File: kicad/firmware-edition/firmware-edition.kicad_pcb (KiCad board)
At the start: 2 copper layers, 109 parts, among them J1 Solar Panel, J10 GPIO, J11 I2C-3V3, J12 GPIO, J13 SPI, J14 I2C-5V, J15 SWD, J16 Conn_01x01_Pin, J17 Conn_01x01_Pin, J18 Conn_01x01_Pin, J19 Conn_01x01_Pin, J2 BATT, J20 Conn_01x01_Pin, J21 GPIO, J3 3V3 Sensor Bus, J4 USB_C_Receptacle_USB2.0_16P, J5 Conn_01x01_Pin, J6 Conn_01x01_Pin, J7 Conn_01x01_Socket, J8 GPIO, J9 Conn_01x01_Pin, Q1 BSS84, Q2 BSS84, Q3 BSS84, SW1 BOOT_DFU, SW2 RST, U1 ADP5091, U2 TPS61023DRLR, U3 MAX-M10M-00B, U4 Si4463, U5 STM32U073KCU6, U6 TXS0102VDCTR, Y1 30MHz

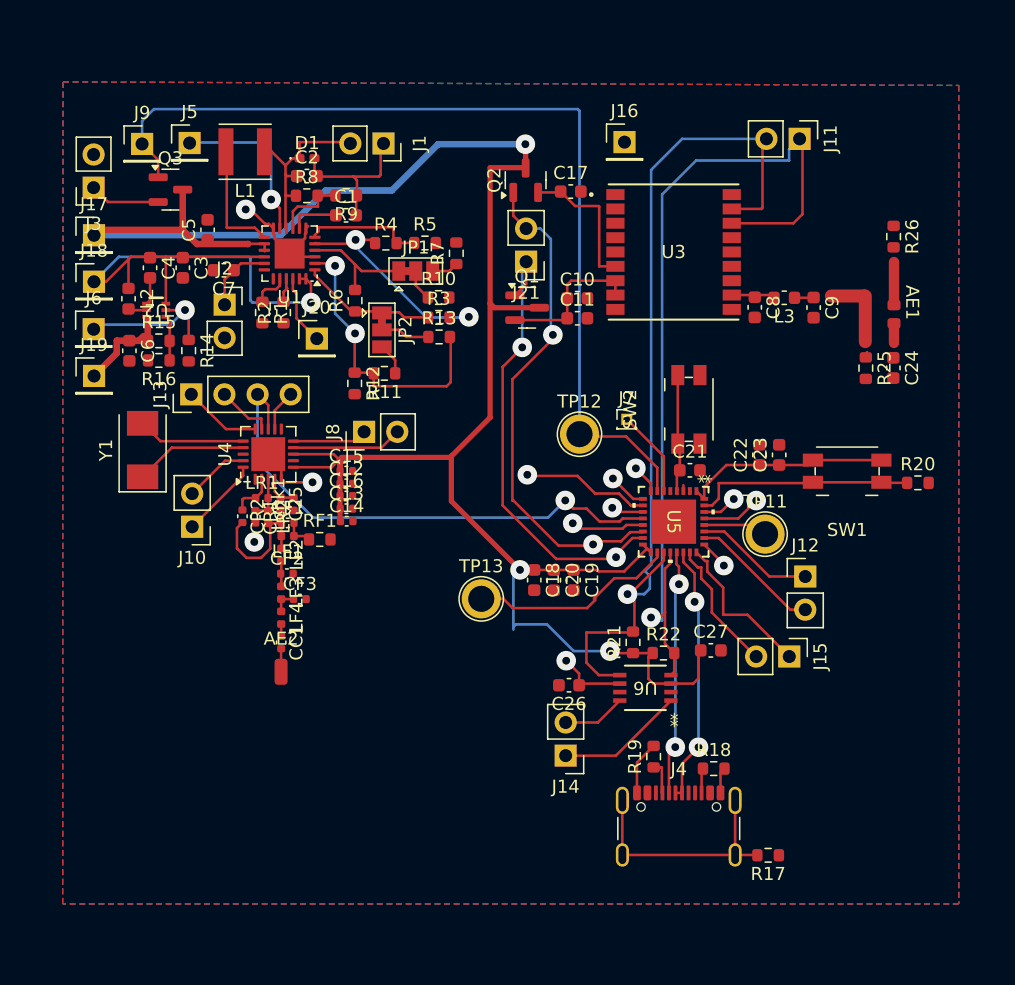
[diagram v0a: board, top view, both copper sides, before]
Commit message: Finished PCB layoiut of Integration board V1.01
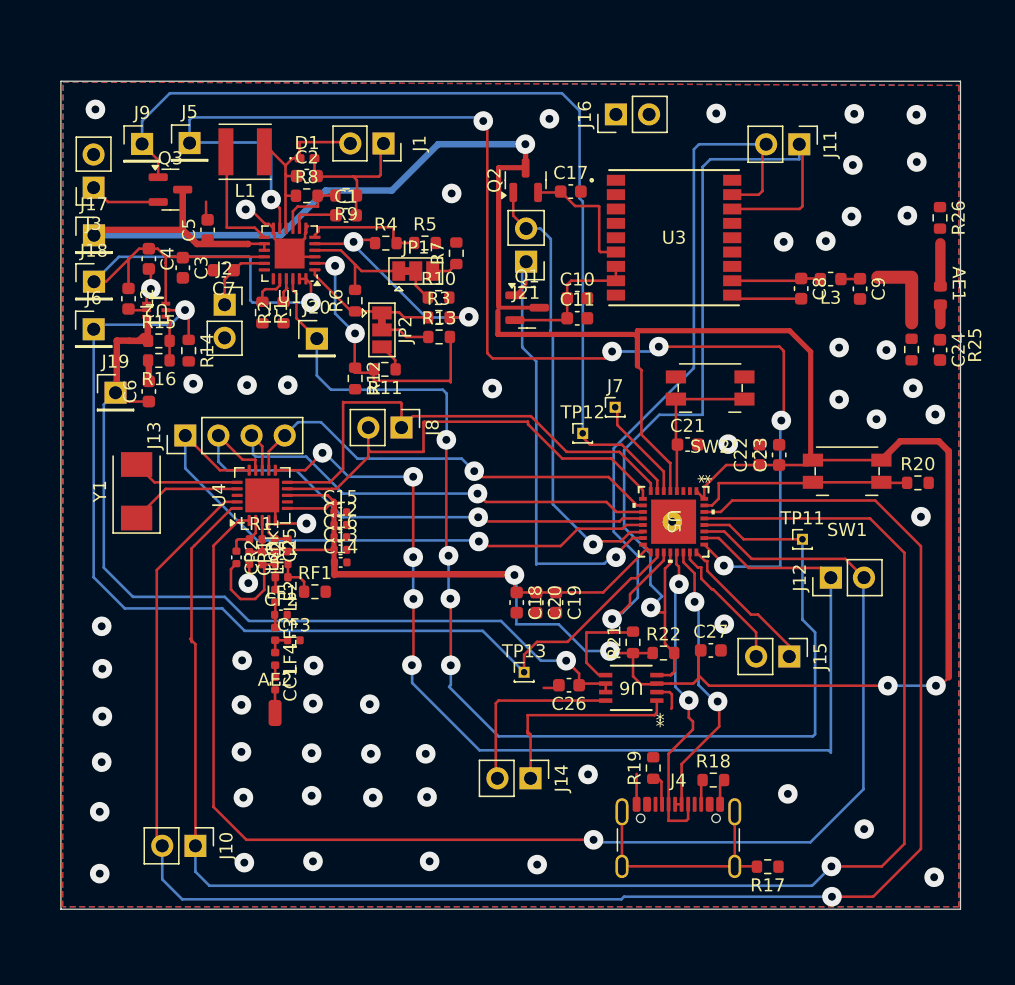
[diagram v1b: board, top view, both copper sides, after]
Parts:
- J16: footprint Connector_PinHeader_2.54mm:PinHeader_1x01_P2.54mm_Vertical -> Connector_PinHeader_2.54mm:PinHeader_1x02_P2.54mm_Vertical
- TP11, TP12, TP13: footprint TestPoint:TestPoint_Plated_Hole_D2.0mm -> Connector_PinHeader_1.00mm:PinHeader_1x01_P1.00mm_Vertical
- moved J10 24.5 mm to (120.3, 123.0), turned to -90 degrees
- moved TP13 6.51 mm to (145.5, 109.7)
- moved RF1 4.02 mm to (129.4, 103.6)
- moved AE1 3.83 mm to (175.1, 80.0)
- moved C8 3.83 mm to (166.7, 80.3)
- moved C9 3.83 mm to (171.2, 80.3)
- moved L3 3.83 mm to (169.0, 79.6)
- moved R26 3.83 mm to (177.3, 74.9)
- moved C24 3.83 mm to (177.3, 85.0)
- moved R25 3.78 mm to (175.2, 85.0)
- moved C6 3.45 mm to (116.7, 88.2), turned to 90 degrees
- moved J14 3.20 mm to (146.0, 117.9), turned to -90 degrees
- moved AE2 3.19 mm to (126.4, 112.8)
- moved C13 3.19 mm to (131.4, 100.3)
- moved C25 3.19 mm to (126.4, 100.0)
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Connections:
- U5 pad 10: ~{RF_CS} -> SCLK
- U5 pad 11: SCLK -> MISO
- U5 pad 12: MISO -> MOSI
- U5 pad 13: MOSI -> ~{RF_CS}
- U5 pad 26: ~{RF_EN} -> ~{RF_IRQ}
- U5 pad 27: ~{RF_IRQ} -> ~{RF_EN}
- U5 pad 29: GPIO2 -> GPIO3
- U5 pad 30: GPIO3 -> GPIO2
- U5 pad 8: GPIO0 -> GPIO1
- U5 pad 9: GPIO1 -> GPIO0
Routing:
- net GPIO2: track 9.50 -> 134.2 mm
- net GPIO3: track 8.85 -> 124.8 mm
- net ~{RF_EN}: track 10.0 -> 106.1 mm, vias 0 -> 1
- net LLD: track 15.0 -> 101.8 mm, vias 2 -> 6
- net ~{CHRGR_EN}: track 10.3 -> 94.4 mm, vias 0 -> 4
- net +3.3V: track 174.2 -> 255.5 mm, vias 3 -> 5
- net ~{RF_IRQ}: track 9.17 -> 86.2 mm, vias 0 -> 5
- net +5V: track 13.5 -> 68.3 mm
- net 5V_EN: track 27.5 -> 81.5 mm
- net ~{RF_CS}: track 15.8 -> 47.1 mm
- net MOSI: track 10.1 -> 40.9 mm
- net GPIO1: track 8.66 -> 38.4 mm, vias 1 -> 0
- net SCLK: track 5.65 -> 33.7 mm
- net GPIO0: track 10.7 -> 35.8 mm, vias 1 -> 0
- net GND: track 34.9 -> 47.5 mm, vias 3 -> 56
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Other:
- board outline added: 68.9 x 63.5 mm

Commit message: slight changes to mainboard, rf0603 layout
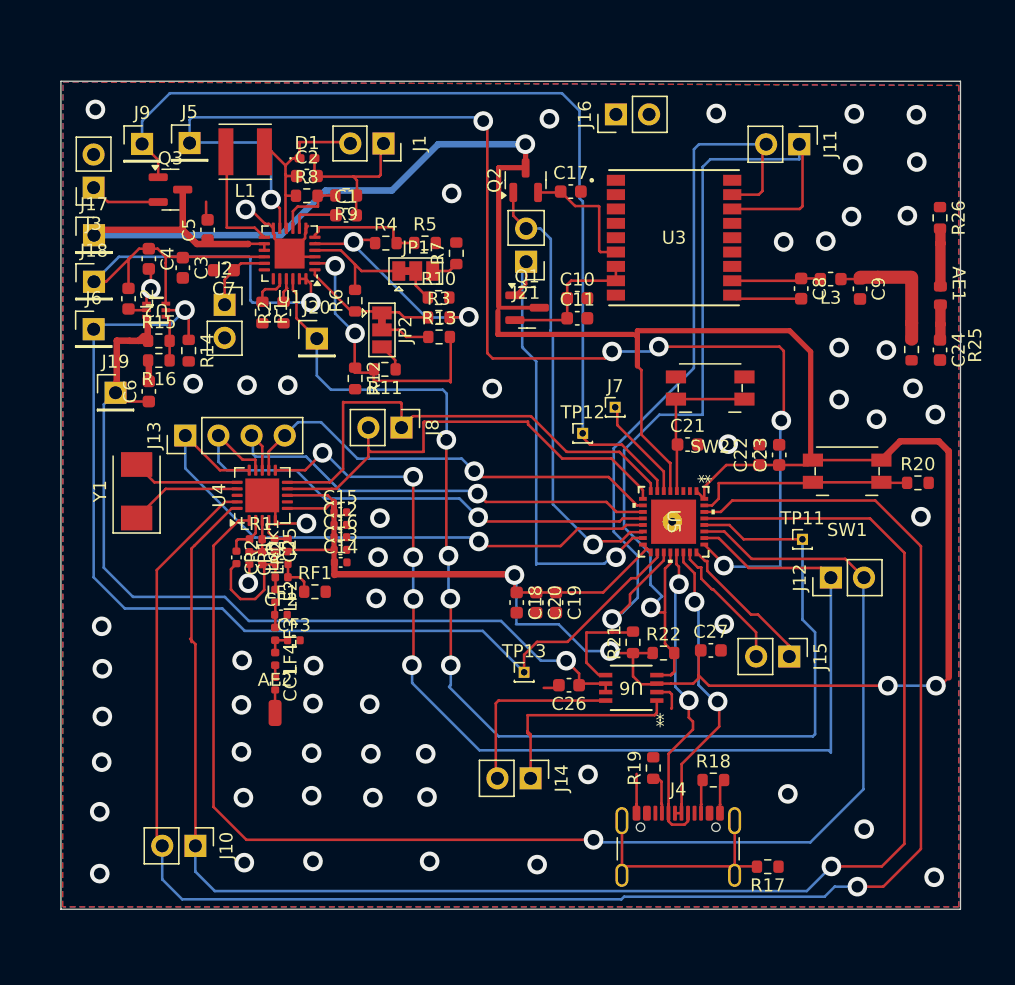
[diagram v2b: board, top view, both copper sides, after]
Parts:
- moved J4 0.68 mm to (157.3, 124.2)
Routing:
- net GND: track 47.5 -> 48.8 mm, vias 56 -> 59
- net Net-(J4-CC2): track 1.75 -> 2.44 mm
- net Net-(U5-PA12[PA10]): track 22.3 -> 22.9 mm
- net Net-(J4-CC1): track 2.48 -> 3.15 mm

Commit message: improved layout, added PGOOD to MCU connection
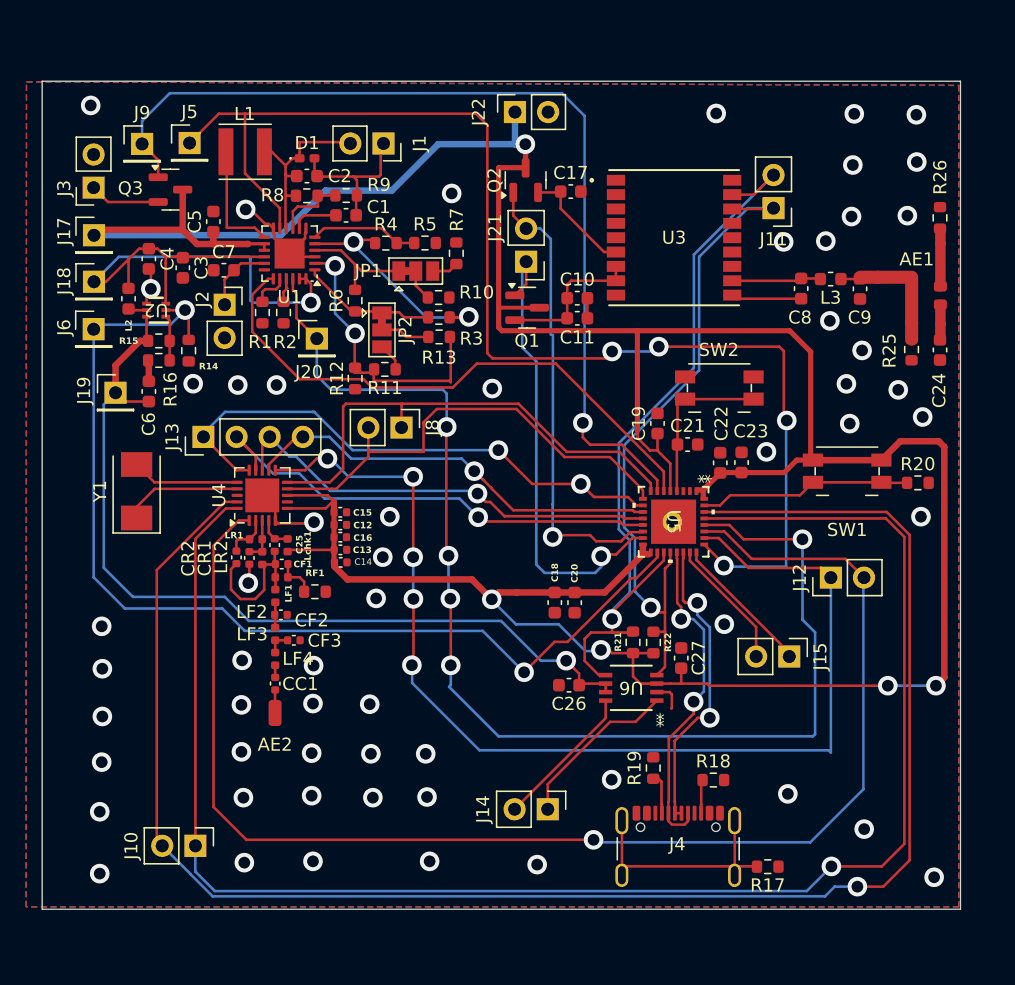
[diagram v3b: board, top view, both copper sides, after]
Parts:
- removed J16: Conn_01x01_Pin, Connector_PinHeader_2.54mm:PinHeader_1x02_P2.54mm_Vertical
- removed J7: Conn_01x01_Socket, Connector_PinHeader_1.00mm:PinHeader_1x01_P1.00mm_Vertical
- removed TP11, TP12, TP13: TestPoint, Connector_PinHeader_1.00mm:PinHeader_1x01_P1.00mm_Vertical
- added J22: 3V3, Connector_PinSocket_2.54mm:PinSocket_1x02_P2.54mm_Vertical, F.Cu at (144.8, 66.8)
- moved C19 15.8 mm to (155.7, 90.7), turned to 90 degrees
- moved J11 5.28 mm to (164.6, 74.2), turned to 180 degrees
- moved C22 3.07 mm to (160.5, 93.7)
- moved C23 2.94 mm to (162.1, 93.7)
- moved C20 2.94 mm to (149.4, 104.4)
- moved C18 2.92 mm to (147.8, 104.4)
- moved J14 2.71 mm to (147.3, 120.2)
- moved C27 2.35 mm to (157.5, 108.6), turned to 90 degrees
- moved J13 1.39 mm to (120.9, 91.7)
- moved R22 1.11 mm to (155.4, 107.5), turned to 90 degrees
- moved C5 0.78 mm to (121.7, 75.2)
- moved SW2 0.70 mm to (160.4, 88.0)
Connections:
- net Net-(U5-PA11[PA9]) renamed /USB_D-
- net Net-(U5-PA12[PA10]) renamed /USB_D+
- U1 pad 19: unconnected-(U1-PGOOD-Pad19) -> PGOOD
- U5 pad 10: SCLK -> ~{RF_CS}
- U5 pad 11: MISO -> SCLK
- U5 pad 12: MOSI -> MISO
- U5 pad 13: ~{RF_CS} -> MOSI
- U5 pad 34: GND -> (no net)
- U5 pad 6: Net-(J7-Pin_1) -> PGOOD
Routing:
- net PGOOD: track 0.00 -> 43.9 mm
- net GPS_SDA: track 71.4 -> 52.5 mm
- net GPS_SCL: track 68.8 -> 58.9 mm
- net Net-(J7-Pin_1): track 7.97 -> 0.00 mm
- net GND: track 48.8 -> 43.1 mm, vias 59 -> 58
- net ~{RF_CS}: track 47.1 -> 41.9 mm, vias 1 -> 2
- net MOSI: track 40.9 -> 37.6 mm
- net /SDA_5V: track 16.2 -> 12.9 mm
- net LLD: track 101.8 -> 98.6 mm, vias 6 -> 4
- net GPIO2: track 134.5 -> 131.4 mm
- net /SCL_5V: track 14.3 -> 11.2 mm
- net +3.3V: track 255.5 -> 253.2 mm
- net MISO: track 36.2 -> 34.0 mm
- net Net-(Q2-S): track 9.90 -> 8.67 mm
- net /USB_D-: track 24.5 -> 25.5 mm
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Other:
- board size 68.9 x 63.5 mm -> 70.4 x 63.5 mm

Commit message: Integration Board V3
Replaced USB C receptacle with Pinout for breakout board, Solved all thermal issues, VSS = GND for STM microcontroller, updated transceiver module to 0603 pads for RLC components
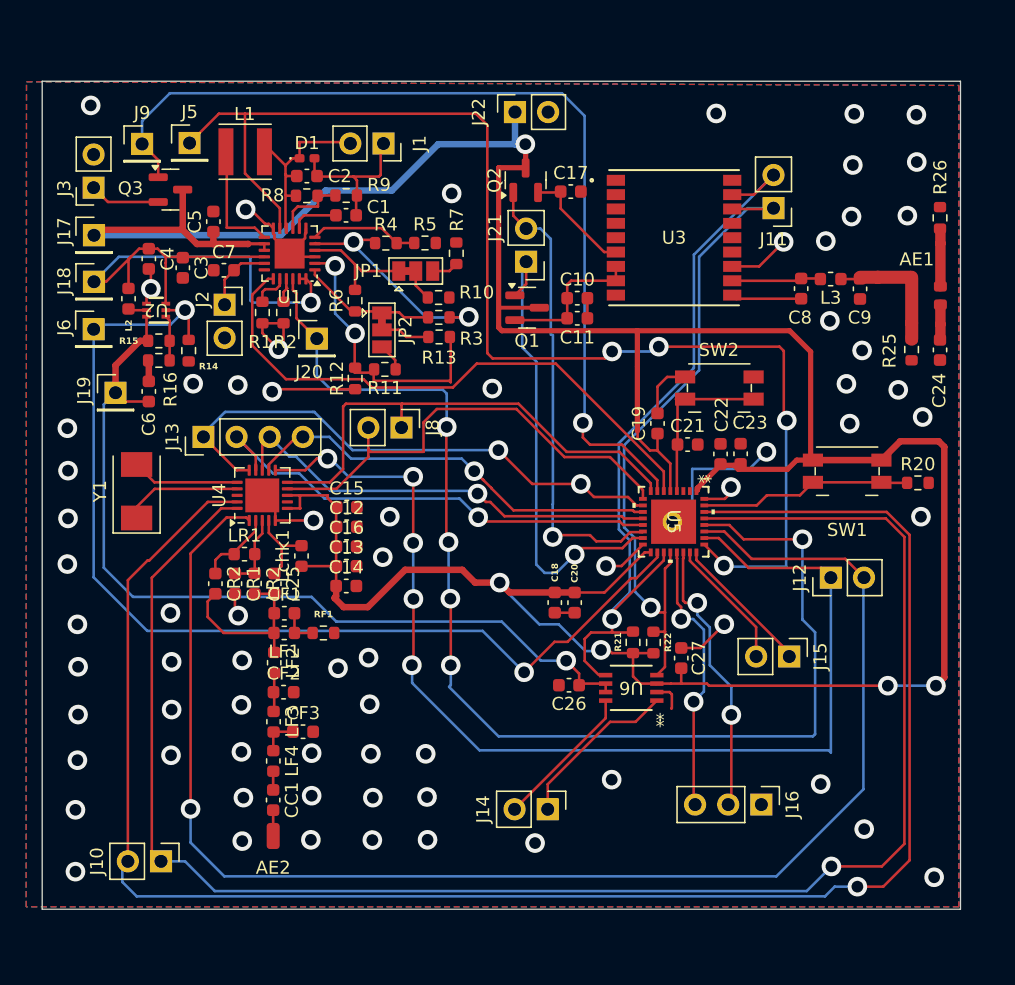
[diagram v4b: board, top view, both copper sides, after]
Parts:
- removed J4: USB_C_Receptacle_USB2.0_16P, Connector_USB:USB_C_Receptacle_GCT_USB4105-xx-A_16P_TopMnt_Horizontal
- removed R17: 0, Resistor_SMD:R_0603_1608Metric
- removed R18, R19: 5.1k, Resistor_SMD:R_0603_1608Metric
- added J16: Conn_01x03, Connector_PinHeader_2.54mm:PinHeader_1x03_P2.54mm_Vertical, F.Cu at (163.7, 119.9)
- C12, C13, C14, C15, C16, C25, CC1, CF1, CF2, CF3, CR1, CR2: footprint Capacitor_SMD:C_0402_1005Metric -> Capacitor_SMD:C_0603_1608Metric
- LF1, LF2, LF3, LF4, LR1, LR2, Lchk1: footprint Inductor_SMD:L_0402_1005Metric -> Inductor_SMD:L_0603_1608Metric
- moved AE2 9.43 mm to (126.2, 122.3)
- moved CC1 8.92 mm to (126.2, 119.5)
- moved LF4 7.82 mm to (126.3, 116.5)
- moved CF3 7.04 mm to (128.5, 114.3)
- moved LF3 6.73 mm to (126.3, 113.5)
- moved CF2 5.93 mm to (127.0, 111.3)
- moved LF2 5.12 mm to (126.3, 109.0)
- moved LF1 4.27 mm to (127.1, 106.7)
- moved CF1 3.77 mm to (127.1, 105.2)
- moved RF1 3.22 mm to (130.1, 106.7)
- moved C25 2.96 mm to (126.3, 102.9)
- moved J10 2.89 mm to (117.7, 124.2)
- moved CR2 2.58 mm to (121.8, 102.9)
- moved CR1 2.26 mm to (123.3, 102.9)
- moved LR2 2.03 mm to (124.8, 102.9)
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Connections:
- U5 pad 16: +3.3V -> GND
- U5 pad 32: +3.3V -> GND
- U5 pad 34: (no net) -> GND
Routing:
- net GND: track 43.1 -> 87.8 mm, vias 58 -> 69
- net Net-(J4-SHIELD): track 18.7 -> 0.00 mm
- net ~{RF_EN}: track 106.1 -> 113.2 mm
- net GPIO2: track 131.4 -> 137.8 mm
- net +3.3V: track 253.2 -> 247.0 mm
- net /USB_D-: track 25.5 -> 21.1 mm
- net GPIO3: track 125.6 -> 129.6 mm
- net Net-(U4-TX): track 2.58 -> 6.23 mm
- net Net-(J4-CC1): track 3.15 -> 0.00 mm
- net Net-(J4-CC2): track 2.44 -> 0.00 mm
- net Net-(U4-RXp): track 3.50 -> 5.93 mm
- net Net-(U4-RXn): track 3.40 -> 5.80 mm
- net Net-(C25-Pad2): track 11.3 -> 13.6 mm
- net /USB_D+: track 23.5 -> 21.8 mm
- net Net-(CF3-Pad1): track 1.90 -> 2.93 mm
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
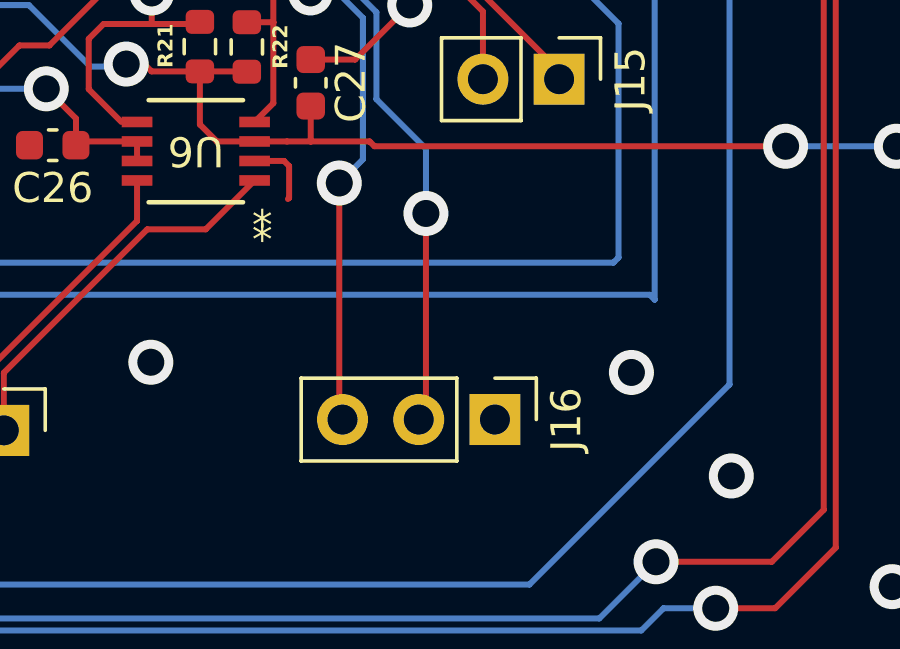
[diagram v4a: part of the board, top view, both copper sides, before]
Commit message: USB C Breakout boards inhouse
Breakout boards for usb C 2.0
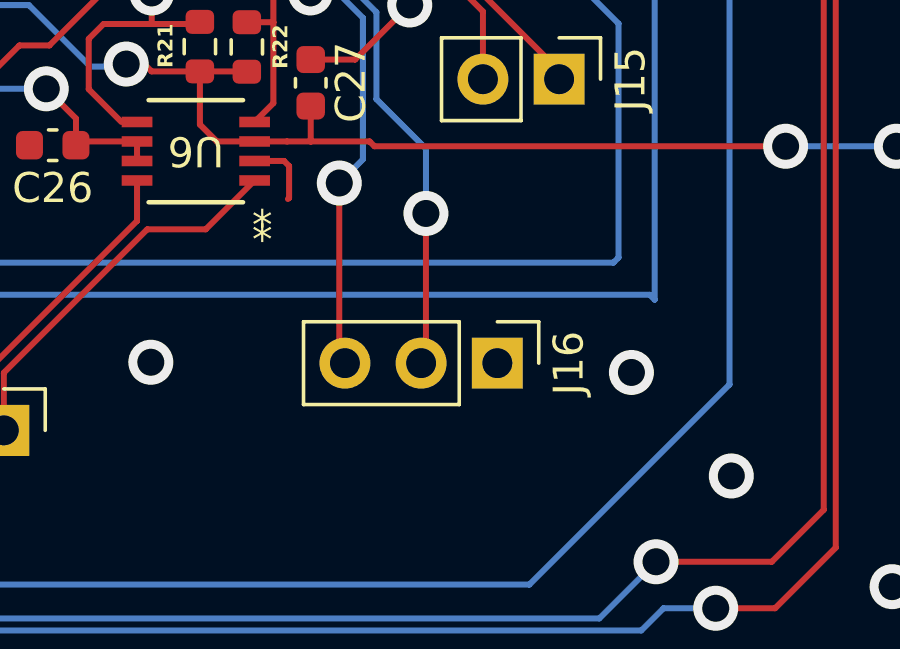
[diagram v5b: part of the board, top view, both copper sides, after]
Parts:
- moved J16 1.88 mm to (163.7, 118.0)
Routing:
- net /USB_D+: track 21.8 -> 19.9 mm
- net /USB_D-: track 21.1 -> 19.3 mm
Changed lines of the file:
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@@
 	(footprint "Connector_PinHeader_2.54mm:PinHeader_1x03_P2.54mm_Vertical"
 		(layer "F.Cu")
-		(at 163.66 119.87 -90)
+		(at 163.74 117.99 -90)
 		(descr "Through hole straight pin header, 1x03, 2.54mm pitch, single row")
 		(tags "Through hole pin header THT 1x03 2.54mm single row")
@@
 	)
 	(segment
-		(start 157.82948 104.411281)
-		(end 157.660126 104.241927)
+		(start 161.36 113)
+		(end 161.36 117.83)
 		(width 0.2)
 		(layer "F.Cu")
@@
 	)
 	(segment
-		(start 161.36 113)
-		(end 161.36 119.63)
+		(start 157.82948 104.411281)
+		(end 157.660126 104.241927)
 		(width 0.2)
 		(layer "F.Cu")
@@
 	)
 	(segment
-		(start 161.36 119.63)
-		(end 161.12 119.87)
+		(start 161.36 117.83)
+		(end 161.2 117.99)
 		(width 0.2)
 		(layer "F.Cu")
@@
 	)
 	(segment
-		(start 158.472186 119.762186)
-		(end 158.58 119.87)
-		(width 0.2)
-		(layer "F.Cu")
-		(net 75)
-	)
-	(segment
 		(start 157.155 100.575063)
 		(end 157.185063 100.545)
@@
 	)
 	(segment
-		(start 158.472186 111.984812)
-		(end 158.472186 119.762186)
+		(start 157.511281 105.648719)
+		(end 157.511281 104.72948)
 		(width 0.2)
 		(layer "F.Cu")
@@
 	)
 	(segment
-		(start 157.511281 105.648719)
-		(end 157.511281 104.72948)
+		(start 157.511281 104.72948)
+		(end 157.210126 104.428325)
 		(width 0.2)
 		(layer "F.Cu")
@@
 	)
 	(segment
-		(start 157.511281 104.72948)
-		(end 157.210126 104.428325)
+		(start 158.472186 111.984812)
+		(end 158.472186 117.802186)
 		(width 0.2)
 		(layer "F.Cu")
@@
 		(width 0.2)
 		(layer "F.Cu")
+		(net 75)
+	)
+	(segment
+		(start 158.472186 117.802186)
+		(end 158.66 117.99)
+		(width 0.2)
+		(layer "F.Cu")
